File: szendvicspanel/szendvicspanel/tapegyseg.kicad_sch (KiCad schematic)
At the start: 0 parts

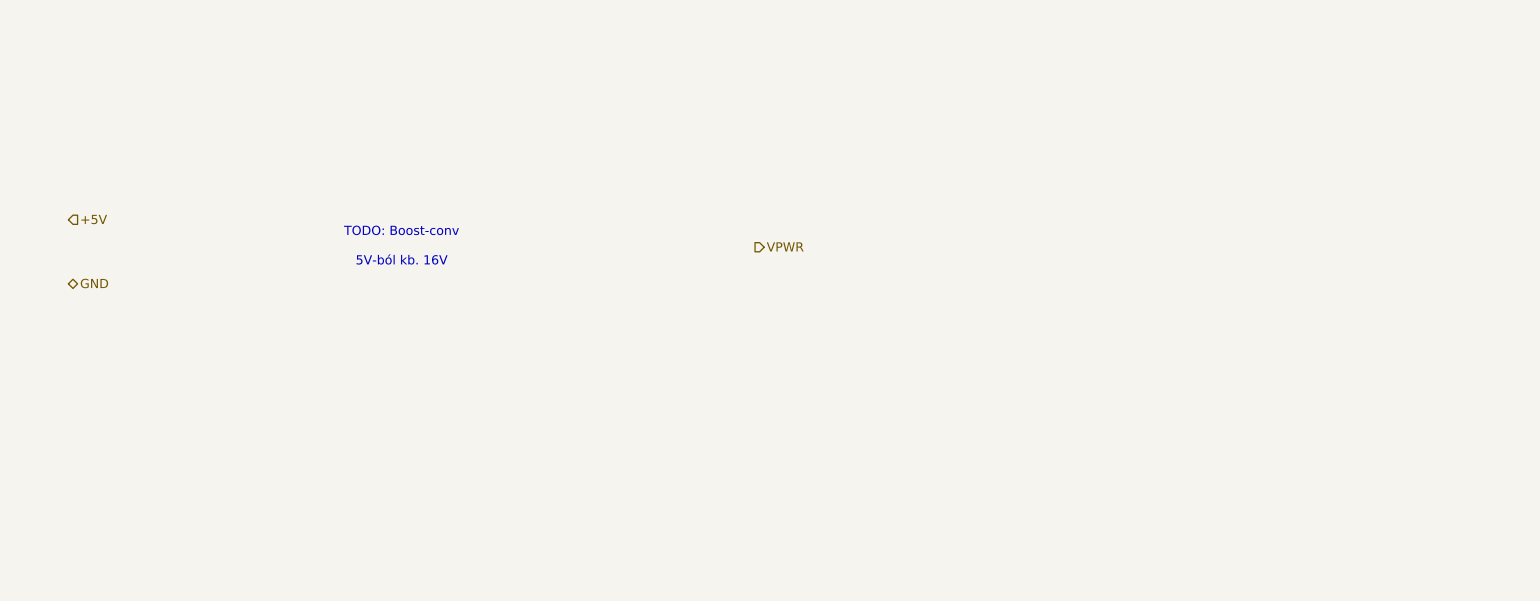
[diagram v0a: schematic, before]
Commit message: Add PSU schematic
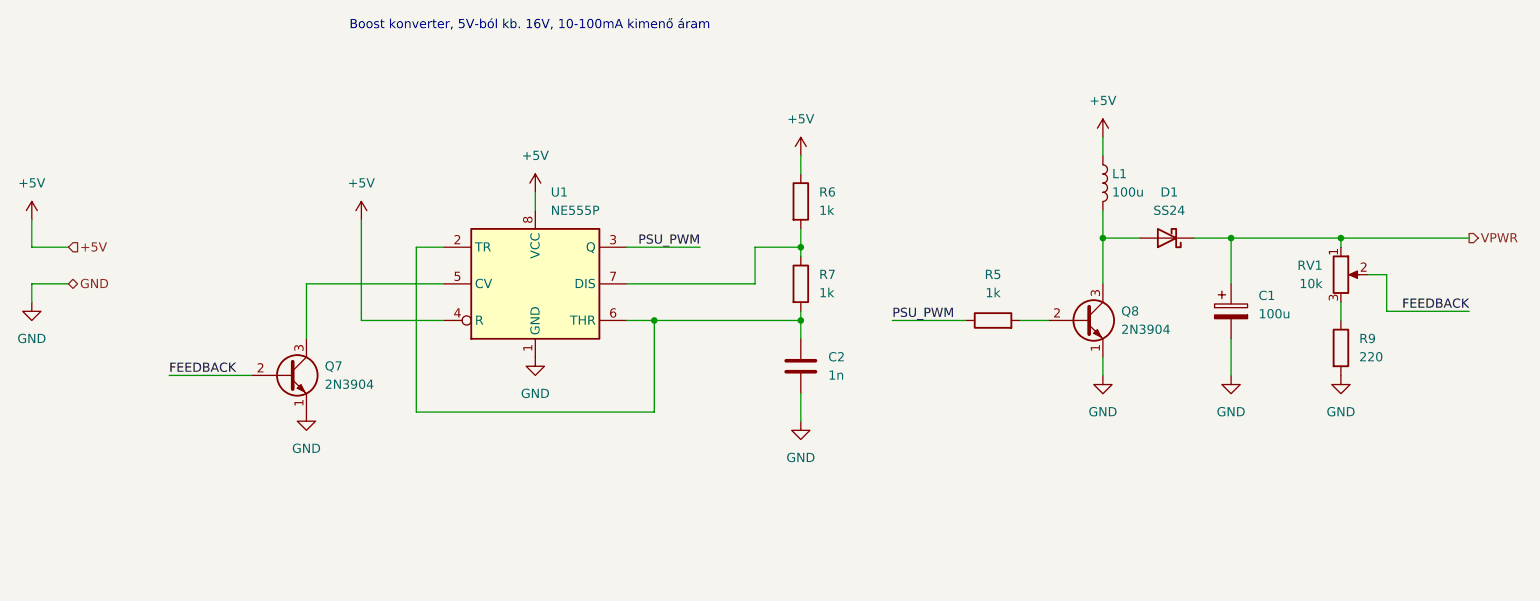
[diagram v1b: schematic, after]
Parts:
- added C1: 100u, symbol Device:C_Polarized
- added C2: 1n, symbol Device:C
- added D1: SS24, Diode_SMD:D_SMA, symbol Diode:SS24
- added L1: 100u, symbol Device:L
- added Q7, Q8: 2N3904, Package_TO_SOT_THT:TO-92_Inline, symbol Transistor_BJT:2N3904
- added R5, R6, R7: 1k, symbol Device:R
- added R9: 220, symbol Device:R
- added RV1: 10k, symbol Device:R_Potentiometer
- added U1: NE555P, Package_DIP:DIP-8_W7.62mm, symbol Timer:NE555P
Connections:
- net +5V: now also L1.1, R6.1, U1.4 (R), U1.8 (VCC)
- net GND: now also C1.2, C2.2, Q7.1 (E), Q8.1 (E), R9.2, U1.1 (GND)
- net VPWR: now also C1.1, D1.1 (K), RV1.1
- new net: R9.1, RV1.3
- new net: C2.1, R7.2, U1.2 (TR), U1.6 (THR)
- new net: D1.2 (A), L1.2, Q8.3 (C)
- new net: Q8.2 (B), R5.2
- new net: Q7.3 (C), U1.5 (CV)
- new net: R6.2, R7.1, U1.7 (DIS)
- new net FEEDBACK: Q7.2 (B), RV1.2
- new net PSU_PWM: R5.1, U1.3 (Q)
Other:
- note added: "Boost konverter, 5V-ból kb. 16V, 10-100mA kimenő áram"
- note removed: "TODO: Boost-conv 5V-ból kb. 16V"

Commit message: Add PSU schematic
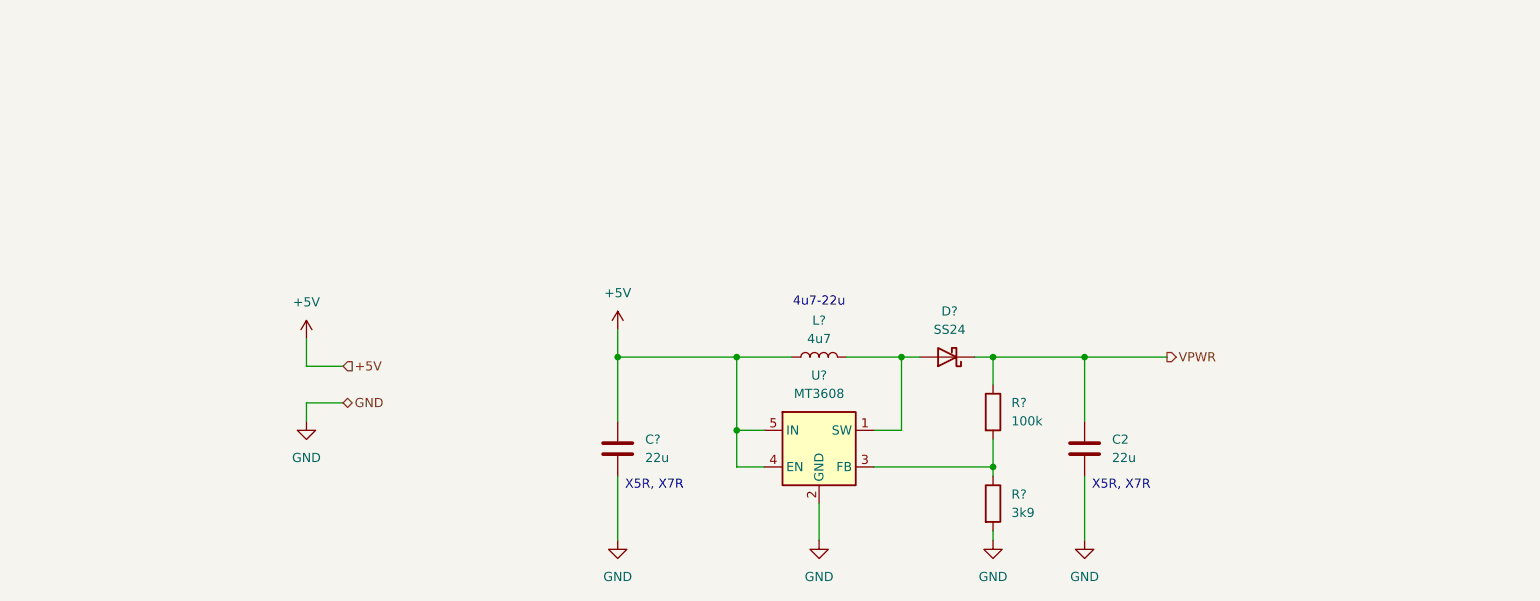
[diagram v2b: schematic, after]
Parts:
- removed C1: 100u, symbol Device:C_Polarized
- removed D1: SS24, Diode_SMD:D_SMA, symbol Diode:SS24
- removed L1: 100u, symbol Device:L
- removed Q7, Q8: 2N3904, Package_TO_SOT_THT:TO-92_Inline, symbol Transistor_BJT:2N3904
- removed R5, R6, R7: 1k, symbol Device:R
- removed R9: 220, symbol Device:R
- removed RV1: 10k, symbol Device:R_Potentiometer
- removed U1: NE555P, Package_DIP:DIP-8_W7.62mm, symbol Timer:NE555P
- added C?: 22u, symbol Device:C
- added D?: SS24, Diode_SMD:D_SMA, symbol Diode:SS24
- added L?: 4u7, symbol Device:L
- added R?: 3k9, symbol Device:R
- added R?: 100k, symbol Device:R
- added U?: MT3608, Package_TO_SOT_SMD:SOT-23-6, symbol Regulator_Switching:MT3608
- C2: value 1n -> 22u
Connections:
- net +5V: now also C?.1, L?.1, U?.4 (EN), U?.5 (IN)
- net GND: now also C?.2, R?.2, U?.2 (GND)
- net VPWR: now also C2.1, D?.1 (K), R?.1
- new net: D?.2 (A), L?.2, U?.1 (SW)
- new net: R?.1, R?.2, U?.3 (FB)
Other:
- note added: "4u7-22u"
- note added: "X5R, X7R"
- note removed: "Boost konverter, 5V-ból kb. 16V, 10-100mA kimenő áram"
- moved on the sheet: C2

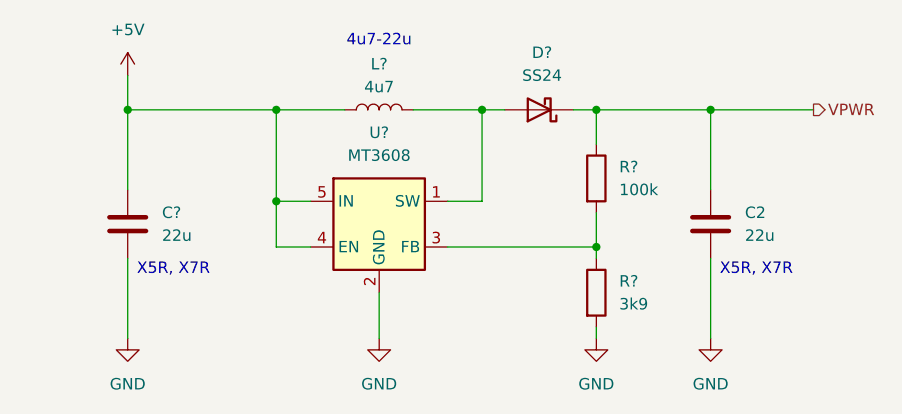
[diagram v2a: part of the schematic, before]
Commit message: Add +5V output to psu.sch
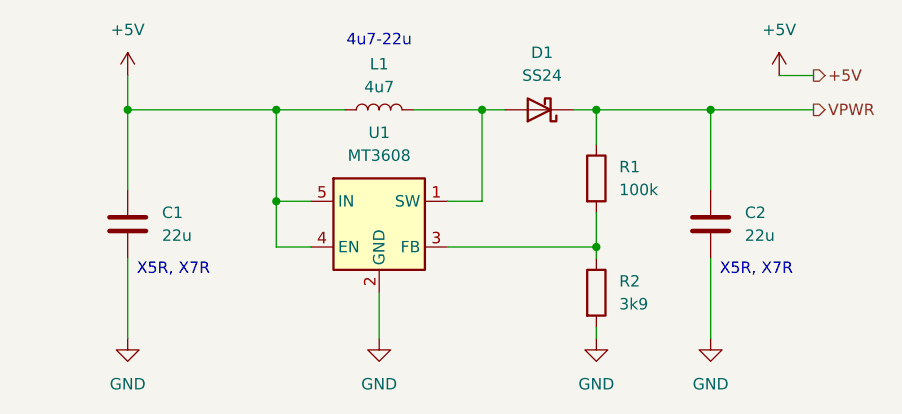
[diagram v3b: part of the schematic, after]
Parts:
- gave numbers to parts that had none: 6
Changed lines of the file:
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@@
+	(wire
+		(pts
+			(xy 194.31 83.82) (xy 198.12 83.82)
+		)
+		(stroke
+			(width 0)
+			(type default)
+		)
+	)
 	(wire
 		(pts
@@
 			(width 0)
 			(type default)
+		)
+	)
+	(hierarchical_label "+5V"
+		(shape output)
+		(at 198.12 83.82 0)
+		(effects
+			(font
+				(size 1.27 1.27)
+			)
+			(justify left)
 		)
 	)
@@
 		(dnp no)
 		(fields_autoplaced yes)
-		(property "Reference" "D?"
+		(property "Reference" "D1"
 			(at 167.9575 81.28 0)
 			(effects
@@
 		(dnp no)
 		(fields_autoplaced yes)
-		(property "Reference" "#PWR?"
+		(property "Reference" "#PWR02"
 			(at 121.92 119.38 0)
 			(effects
@@
 		(dnp no)
 		(fields_autoplaced yes)
-		(property "Reference" "C2"
+		(property "Reference" "C?"
 			(at 190.5 99.0599 0)
 			(effects
@@
 		(dnp no)
 		(fields_autoplaced yes)
-		(property "Reference" "#PWR015"
+		(property "Reference" "#PWR?"
 			(at 78.74 88.9 0)
 			(effects
@@
 		(dnp no)
 		(fields_autoplaced yes)
-		(property "Reference" "U?"
+		(property "Reference" "U1"
 			(at 149.86 90.17 0)
 			(effects
@@
 		(dnp no)
 		(fields_autoplaced yes)
-		(property "Reference" "R?"
+		(property "Reference" "R2"
 			(at 176.53 106.6799 0)
 			(effects
@@
 	(symbol
 		(lib_id "power:+5V")
+		(at 194.31 83.82 0)
+		(unit 1)
+		(exclude_from_sim no)
+		(in_bom yes)
+		(on_board yes)
+		(dnp no)
+		(fields_autoplaced yes)
+		(property "Reference" "#PWR06"
+			(at 194.31 87.63 0)
+			(effects
+				(font
+					(size 1.27 1.27)
+				)
+				(hide yes)
+			)
+		)
+		(property "Value" "+5V"
+			(at 194.31 78.74 0)
+			(effects
+				(font
+					(size 1.27 1.27)
+				)
+			)
+		)
+		(property "Footprint" ""
+			(at 194.31 83.82 0)
+			(effects
+				(font
+					(size 1.27 1.27)
+				)
+				(hide yes)
+			)
+		)
+		(property "Datasheet" ""
+			(at 194.31 83.82 0)
+			(effects
+				(font
+					(size 1.27 1.27)
+				)
+				(hide yes)
+			)
+		)
+		(property "Description" "Power symbol creates a global label with name \"+5V\""
+			(at 194.31 83.82 0)
+			(effects
+				(font
+					(size 1.27 1.27)
+				)
+				(hide yes)
+			)
+		)
+		(pin "1"
+		)
+		(instances
+			(project "tapegyseg"
+				(path "/f7670cfa-9c8c-4aa4-91d3-ead739118674"
+					(reference "#PWR06")
+					(unit 1)
+				)
+			)
+		)
+	)
+	(symbol
+		(lib_id "power:+5V")
 		(at 121.92 83.82 0)
 		(unit 1)
@@
 		(dnp no)
 		(fields_autoplaced yes)
-		(property "Reference" "#PWR?"
+		(property "Reference" "#PWR05"
 			(at 121.92 87.63 0)
 			(effects
@@
 		(dnp no)
 		(fields_autoplaced yes)
-		(property "Reference" "#PWR?"
+		(property "Reference" "#PWR01"
 			(at 149.86 119.38 0)
 			(effects
@@
 		(dnp no)
 		(fields_autoplaced yes)
-		(property "Reference" "L?"
+		(property "Reference" "L1"
 			(at 149.86 82.55 90)
 			(effects
@@
 		(dnp no)
 		(fields_autoplaced yes)
-		(property "Reference" "#PWR?"
+		(property "Reference" "#PWR04"
 			(at 186.69 119.38 0)
 			(effects
@@
 		(dnp no)
 		(fields_autoplaced yes)
-		(property "Reference" "C?"
+		(property "Reference" "C1"
 			(at 125.73 99.0599 0)
 			(effects
@@
 		(dnp no)
 		(fields_autoplaced yes)
-		(property "Reference" "#PWR?"
+		(property "Reference" "#PWR03"
 			(at 173.99 119.38 0)
 			(effects
@@
 		(dnp no)
 		(fields_autoplaced yes)
-		(property "Reference" "R?"
+		(property "Reference" "R1"
 			(at 176.53 93.9799 0)
 			(effects
@@
 		(dnp no)
 		(fields_autoplaced yes)
-		(property "Reference" "#PWR014"
+		(property "Reference" "#PWR?"
 			(at 78.74 102.87 0)
 			(effects

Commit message: Analóg jelgen schematic copy+paste, output busz, analóg interfész pinjeinek frissítése
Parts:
- renumbered C1 to C?, D1 to D?, L1 to L?, R2 to R?, R1 to R?, U1 to U?
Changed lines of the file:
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@@
 		(dnp no)
 		(fields_autoplaced yes)
-		(property "Reference" "D1"
+		(property "Reference" "D?"
 			(at 167.9575 81.28 0)
 			(effects
@@
 		(dnp no)
 		(fields_autoplaced yes)
-		(property "Reference" "#PWR02"
+		(property "Reference" "#PWR?"
 			(at 121.92 119.38 0)
 			(effects
@@
 		(dnp no)
 		(fields_autoplaced yes)
-		(property "Reference" "C?"
+		(property "Reference" "C2"
 			(at 190.5 99.0599 0)
 			(effects
@@
 		(dnp no)
 		(fields_autoplaced yes)
-		(property "Reference" "#PWR?"
+		(property "Reference" "#PWR015"
 			(at 78.74 88.9 0)
 			(effects
@@
 		(dnp no)
 		(fields_autoplaced yes)
-		(property "Reference" "U1"
+		(property "Reference" "U?"
 			(at 149.86 90.17 0)
 			(effects
@@
 		(dnp no)
 		(fields_autoplaced yes)
-		(property "Reference" "R2"
+		(property "Reference" "R?"
 			(at 176.53 106.6799 0)
 			(effects
@@
 		(dnp no)
 		(fields_autoplaced yes)
-		(property "Reference" "#PWR06"
+		(property "Reference" "#PWR?"
 			(at 194.31 87.63 0)
 			(effects
@@
 		)
 		(instances
+			(project "szendvicspanel"
+				(path "/2e536be4-7a69-4064-ab31-c73232c2dcfe/c1a87f4a-0473-4080-9ef3-9f191c8d170d"
+					(reference "#PWR?")
+					(unit 1)
+				)
+			)
 			(project "tapegyseg"
 				(path "/f7670cfa-9c8c-4aa4-91d3-ead739118674"
@@
 		(dnp no)
 		(fields_autoplaced yes)
-		(property "Reference" "#PWR05"
+		(property "Reference" "#PWR?"
 			(at 121.92 87.63 0)
 			(effects
@@
 		(dnp no)
 		(fields_autoplaced yes)
-		(property "Reference" "#PWR01"
+		(property "Reference" "#PWR?"
 			(at 149.86 119.38 0)
 			(effects
@@
 		(dnp no)
 		(fields_autoplaced yes)
-		(property "Reference" "L1"
+		(property "Reference" "L?"
 			(at 149.86 82.55 90)
 			(effects
@@
 		(dnp no)
 		(fields_autoplaced yes)
-		(property "Reference" "#PWR04"
+		(property "Reference" "#PWR?"
 			(at 186.69 119.38 0)
 			(effects
@@
 		(dnp no)
 		(fields_autoplaced yes)
-		(property "Reference" "C1"
+		(property "Reference" "C?"
 			(at 125.73 99.0599 0)
 			(effects
@@
 		(dnp no)
 		(fields_autoplaced yes)
-		(property "Reference" "#PWR03"
+		(property "Reference" "#PWR?"
 			(at 173.99 119.38 0)
 			(effects
@@
 		(dnp no)
 		(fields_autoplaced yes)
-		(property "Reference" "R1"
+		(property "Reference" "R?"
 			(at 176.53 93.9799 0)
 			(effects
@@
 		(dnp no)
 		(fields_autoplaced yes)
-		(property "Reference" "#PWR?"
+		(property "Reference" "#PWR014"
 			(at 78.74 102.87 0)
 			(effects
